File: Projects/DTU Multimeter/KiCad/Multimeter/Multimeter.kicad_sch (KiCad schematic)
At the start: 10 parts, among them U1 MCP3208-CI_P, U2 CD74HC4067E, U3 CD4053BE, U4 LM358P, U5 LM311N, U6 NE555P, U7 LM35DZ, U8 DS1307+

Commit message: Add schematic generator and update measured resistor values
Add generate_schematic.py using kicad-skip + sexpdata to programmatically
inject all passive components, net labels, power symbols, and group
annotations into the KiCad schematic. Moves existing ICs to a spread-out
layout via raw S-expression tree manipulation. Update config.h and build
guide with actual measured resistor values.
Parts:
- added BT1: CR2032, Battery:BatteryHolder_Keystone_3034_1x20mm, symbol Device:Battery_Cell
- added BZ1: Piezo, Buzzer_Beeper:Buzzer_12x9.5RM7.6, symbol Device:Buzzer
- added C1, C2, C3, C7, C8: 100n, Capacitor_THT:C_Disc_D5.0mm_W2.5mm_P2.50mm, symbol Device:C
- added C4, C5, C6: 10u, Capacitor_THT:CP_Radial_D5.0mm_P2.50mm, symbol Device:C_Polarized
- added D1: Red, LED_THT:LED_D3.0mm, symbol Device:LED
- added D2: Green, LED_THT:LED_D3.0mm, symbol Device:LED
- added D3: Yellow, LED_THT:LED_D3.0mm, symbol Device:LED
- added F1: 10A, Fuse:Fuseholder_Clip-5x20mm_Keystone_3517_Inline_P23.11x6.76mm_D1.70mm_Horizontal, symbol Device:Fuse
- added F2: 500mA, Fuse:Fuseholder_Clip-5x20mm_Keystone_3517_Inline_P23.11x6.76mm_D1.70mm_Horizontal, symbol Device:Fuse
- added R1: 50.15, Resistor_THT:R_Axial_DIN0207_L6.3mm_D2.5mm_P10.16mm_Horizontal, symbol Device:R
- added R10: 998, Resistor_THT:R_Axial_DIN0207_L6.3mm_D2.5mm_P10.16mm_Horizontal, symbol Device:R
- added R11: 99.49, Resistor_THT:R_Axial_DIN0207_L6.3mm_D2.5mm_P10.16mm_Horizontal, symbol Device:R
- added R12: 10.04, Resistor_THT:R_Axial_DIN0207_L6.3mm_D2.5mm_P10.16mm_Horizontal, symbol Device:R
- added R13: 1.05, Resistor_THT:R_Axial_DIN0207_L6.3mm_D2.5mm_P10.16mm_Horizontal, symbol Device:R
- added R14: 0.145, Resistor_THT:R_Axial_DIN0207_L6.3mm_D2.5mm_P10.16mm_Horizontal, symbol Device:R
- added R15: 1.002M, Resistor_THT:R_Axial_DIN0207_L6.3mm_D2.5mm_P10.16mm_Horizontal, symbol Device:R
- added R16: 100k, Resistor_THT:R_Axial_DIN0207_L6.3mm_D2.5mm_P10.16mm_Horizontal, symbol Device:R
- added R17: 1.003M, Resistor_THT:R_Axial_DIN0207_L6.3mm_D2.5mm_P10.16mm_Horizontal, symbol Device:R
- added R18, R22, R23, R24, R28, R29, R9: 10k, Resistor_THT:R_Axial_DIN0207_L6.3mm_D2.5mm_P10.16mm_Horizontal, symbol Device:R
- added R19: 99.48, Resistor_THT:R_Axial_DIN0207_L6.3mm_D2.5mm_P10.16mm_Horizontal, symbol Device:R
- added R2: 497, Resistor_THT:R_Axial_DIN0207_L6.3mm_D2.5mm_P10.16mm_Horizontal, symbol Device:R
- added R20: 9.09k, Resistor_THT:R_Axial_DIN0207_L6.3mm_D2.5mm_P10.16mm_Horizontal, symbol Device:R
- added R21: 1k, Resistor_THT:R_Axial_DIN0207_L6.3mm_D2.5mm_P10.16mm_Horizontal, symbol Device:R
- added R25, R26, R27: 330, Resistor_THT:R_Axial_DIN0207_L6.3mm_D2.5mm_P10.16mm_Horizontal, symbol Device:R
- added R3: 4990, Resistor_THT:R_Axial_DIN0207_L6.3mm_D2.5mm_P10.16mm_Horizontal, symbol Device:R
- added R4: 48.536k, Resistor_THT:R_Axial_DIN0207_L6.3mm_D2.5mm_P10.16mm_Horizontal, symbol Device:R
- added R5: 498k, Resistor_THT:R_Axial_DIN0207_L6.3mm_D2.5mm_P10.16mm_Horizontal, symbol Device:R
- added R6: 4.755M, Resistor_THT:R_Axial_DIN0207_L6.3mm_D2.5mm_P10.16mm_Horizontal, symbol Device:R
- added R7: 10.06M, Resistor_THT:R_Axial_DIN0207_L6.3mm_D2.5mm_P10.16mm_Horizontal, symbol Device:R
- added R8: 10.03M, Resistor_THT:R_Axial_DIN0207_L6.3mm_D2.5mm_P10.16mm_Horizontal, symbol Device:R
- added SW1: MODE, Button_Switch_THT:SW_PUSH_6mm, symbol Switch:SW_Push
- added SW2: FUNC, Button_Switch_THT:SW_PUSH_6mm, symbol Switch:SW_Push
- added SW3: RANGE, Button_Switch_THT:SW_PUSH_6mm, symbol Switch:SW_Push
- added SW4: SELECT, Button_Switch_THT:SW_PUSH_6mm, symbol Switch:SW_Push
- added Y1: 32.768kHz, Crystal:Crystal_C38-LF_D3.0mm_L8.0mm_Horizontal, symbol Device:Crystal
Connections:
- net GND: now reaches U6.1 (GND)
- net GND: now also U7.3 (GND)
- net VCC: now reaches U6.8 (VCC)
- net VCC: now also U7.1 (+VS)
- net ADC_CH5: now reaches U7.2 (VOUT)
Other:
- note added: "ADC (U1 MCP3208)"
- note added: "ANALOG MUX (U2 74HC4067 + Ref R1-R8)"
- note added: "CURRENT MUX (U3 CD4053 + Shunts R9-R14)"
- note added: "CURRENT SOURCE (U6 NE555 + C8, R17-R19)"
- note added: "DECOUPLING (C1-C6 near each IC)"
- note added: "DISPLAY (OLED 128x64, DS)"
- note added: "FREQUENCY COUNTER (U5 LM311 + R22-R24, C7)"
- note added: "I2C BUS (Pull-ups R28-R29)"
- note added: "INPUT PROTECTION (Fuses F1-F2 + Voltage Divider R15-R16)"
- note added: "RTC (U8 DS1307 + Crystal Y1 + Battery BT1)"
- note added: "SIGNAL CONDITIONING (U4 LM358 + R20-R21)"
- note added: "TEMPERATURE (U7 LM35)"
- note added: "USER INTERFACE (Buttons SW1-SW4, LEDs D1-D3, Buzzer BZ1)"
- moved on the sheet: A1, DS1, U1, U2, U3, U4A, U4B, U4C, U5, U6, U7, U8

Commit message: Wire R1-R8, R9-R14 and fix ERC errors
- Wire R1-R8 probe-input side to ADC_CH2 net (bus wire + junctions)
- Wire R9-R14 fuse-terminal side with FUSE_mA/FUSE_10A labels
- Fix ERC: relocate TERM labels, remove orphaned #PWR026,
  add 57 no-connect flags on unused A1 pins, add PWR_FLAG
  symbols on VCC/GND/VBAT nets
- Add schematic wiring guide
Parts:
- added D4: 1N4148, Diode_THT:D_DO-35_SOD27_P7.62mm_Horizontal, symbol Device:D
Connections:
- net ADC_CH1: now also R15.2, R16.1, U1.2 (CH1)
- net ADC_CH2: now also R1.1, R15.1, R2.1, R3.1, R4.1, R5.1, R6.1, R7.1, R8.1, U1.3 (CH2)
- net ADC_CH3: now also R20.2, U1.4 (CH3), U4.1
- net ADC_CH4: now also U1.5 (CH4), U4.7, D4.1 (K)
- net ADC_CH5: now also U1.6 (CH5)
- net BTN_FUNC: now also A1.AD4, SW2.1
- net BTN_MODE: now also A1.AD3, SW1.1
- net BTN_RANGE: now also A1.AD5, SW3.1
- net BTN_SEL: now also A1.AD6, SW4.1
- net BUZZER: now also A1.AD7, BZ1.1 (+)
- net CAP_CHG: now also A1.31, U6.3 (OUT)
- net CAP_DIS: now also A1.32
- net CUR_A: now also A1.27, U3.11 (A)
- net CUR_B: now also A1.28, U3.10 (B)
- net CUR_C: now also A1.29, U3.9 (C)
- net CUR_INH: now also A1.30, U3.6 (INH)
- net FREQ_IN: now also A1.AD2, R24.2, U5.7 (OUT)
- net GND: now also A1.GND2, BT1.2 (-), BZ1.2 (-), C1.2, C2.2, C3.2, C4.2, C5.2, C6.2, C8.2, D1.1 (K), D2.1 (K), D3.1 (K), DS1.2 (GND), R16.2, R21.2, R23.2, SW1.2, SW2.2, SW3.2, SW4.2, U1.14 (AGND), U1.9 (DGND), U2.12 (GND), U3.7 (VEE), U3.8 (VSS), U4.4 (GND), U5.1 (GND), U5.4 (VCC-), U8.4 (GND)
- net I2C_SCL: now also A1.SCL, DS1.3 (SCK), R29.2, U8.6 (SCL)
- net I2C_SDA: now also A1.SDA, DS1.4 (SDA), R28.2, U8.5 (SDA)
- net ISRC_EN: now also A1.33, U6.4 (RESET)
- net LED_GRN: now also A1.AD9, R26.1
- net LED_RED: now also A1.AD8, R25.1
- net LED_YEL: now also A1.AD10, R27.1
- net MUX_COM: now also U1.1 (CH0), U2.1 (COM)
- net MUX_EN: now also A1.26, U2.15 (~{E})
- net MUX_S0: now also A1.22, U2.10 (S0)
- net MUX_S1: now also A1.23, U2.11 (S1)
- net MUX_S2: now also A1.24, U2.14 (S2)
- net MUX_S3: now also A1.25, U2.13 (S3)
- net SPI_CS: now also A1.53, U1.10 (~CS/SHDN)
- net SPI_MISO: now also A1.50, U1.12 (DOUT)
- net SPI_MOSI: now also A1.51, U1.11 (DIN)
- net SPI_SCK: now also A1.52, U1.13 (CLK)
- net VCC: now also A1.5V_1 (+5V_1), C1.1, C2.1, C3.1, C4.1, C5.1, C6.1, DS1.1 (VDD), R22.1, R24.1, R28.1, R29.1, U1.15 (VREF), U1.16 (VDD), U2.24 (VCC), U3.16 (VDD), U4.8 (VCC), U5.8 (VCC+), U8.8 (VCC)
- net at R1.2: now also U2.9 (I0)
- net at D3.2 (A): now also R27.2
- net at C7.1: now also U5.2 (POS)
- net at U2.2 (I7): now also R8.2
- net at U2.3 (I6): now also R7.2
- net at U2.4 (I5): now also R6.2
- net at U2.5 (I4): now also R5.2
- net at U2.6 (I3): now also R4.2
- net at U2.7 (I2): now also R3.2
- net at U2.8 (I1): now also R2.2
- net FUSE_mA: now reaches R9.1
- net FUSE_mA: now also F2.2, R10.1, R11.2, R12.1, R13.1
- net at R9.2: now also U3.12 (AX_IN/OUT)
- net at D1.2 (A): now also R25.2
- net at R12.2: now also U3.3 (IN/OUT_CY)
- net at C8.1: now also U6.5 (CONT)
- net TMR_CAP: now reaches R18.2
- net TMR_CAP: now also R17.2, R19.2, U6.2 (TRIG), U6.6 (THRES)
- net at R17.1: now also R19.1, U6.7 (DISCH)
- net at D2.2 (A): now also R26.2
- net TERM_10A: now reaches F1.1
- net FUSE_10A: now reaches F1.2
- net FUSE_10A: now also R14.1
- net at R10.2: now also U3.13 (AY_IN/OUT)
- net at R20.1: now also R21.1, U4.2
- net at U4.6: now also D4.2 (A)
- net at R14.2: now also U3.1 (IN/OUT_BY)
- net at R23.1: now also R22.2, U5.3 (NEG)
- net at Y1.1: now also U8.2 (X2)
- net at Y1.2: now also U8.1 (X1)
- net SHUNT_NODE: now reaches U3.14 (OUT/IN_AX_OR_AY)
- net SHUNT_NODE: now also U3.15 (OUT/IN_BX_OR_BY), U3.4 (OUT/IN_CX_OR_CY), U4.3
- net at U3.2 (IN/OUT_BX): now also R13.2
- net at U3.5 (IN/OUT_CX): now also R11.1
- net at U8.3 (VBAT): now also BT1.1 (+)
- net TERM_mA: now reaches F2.1
- no-connect marks 0 -> 70
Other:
- moved on the sheet: BZ1, C2, C3, C4, C5, C6, C8, D1, D2, D3, F1, F2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

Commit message: Update DTU Multimeter PCB layout, schematic, and build guide
Add KiCad schematic fix scripts, ERC report, design plans,
and PlatformIO project configuration.
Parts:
- added J1, J2: Conn_01x01_Pin, Connector:Banana_Jack_1Pin, symbol Connector:Conn_01x01_Pin
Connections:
- net TMR_CAP is gone; now on net CAP_DIS: R17.2, R18.2, R19.2, U6.2 (TRIG), U6.6 (THRES)
- net ADC_CH2: now also C7.2, U4.5
- net ADC_CH4: now also D4.2 (A), U4.6
- net TERM_10A: now also J1.1 (Pin_1)
- net TERM_mA: now also J2.1 (Pin_1)
- net at R18.1: now also R17.1, R19.1, U6.7 (DISCH)
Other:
- moved on the sheet: A1, BT1, BZ1, C1, C2, C3, C4, C5, C6, C7, C8, D1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

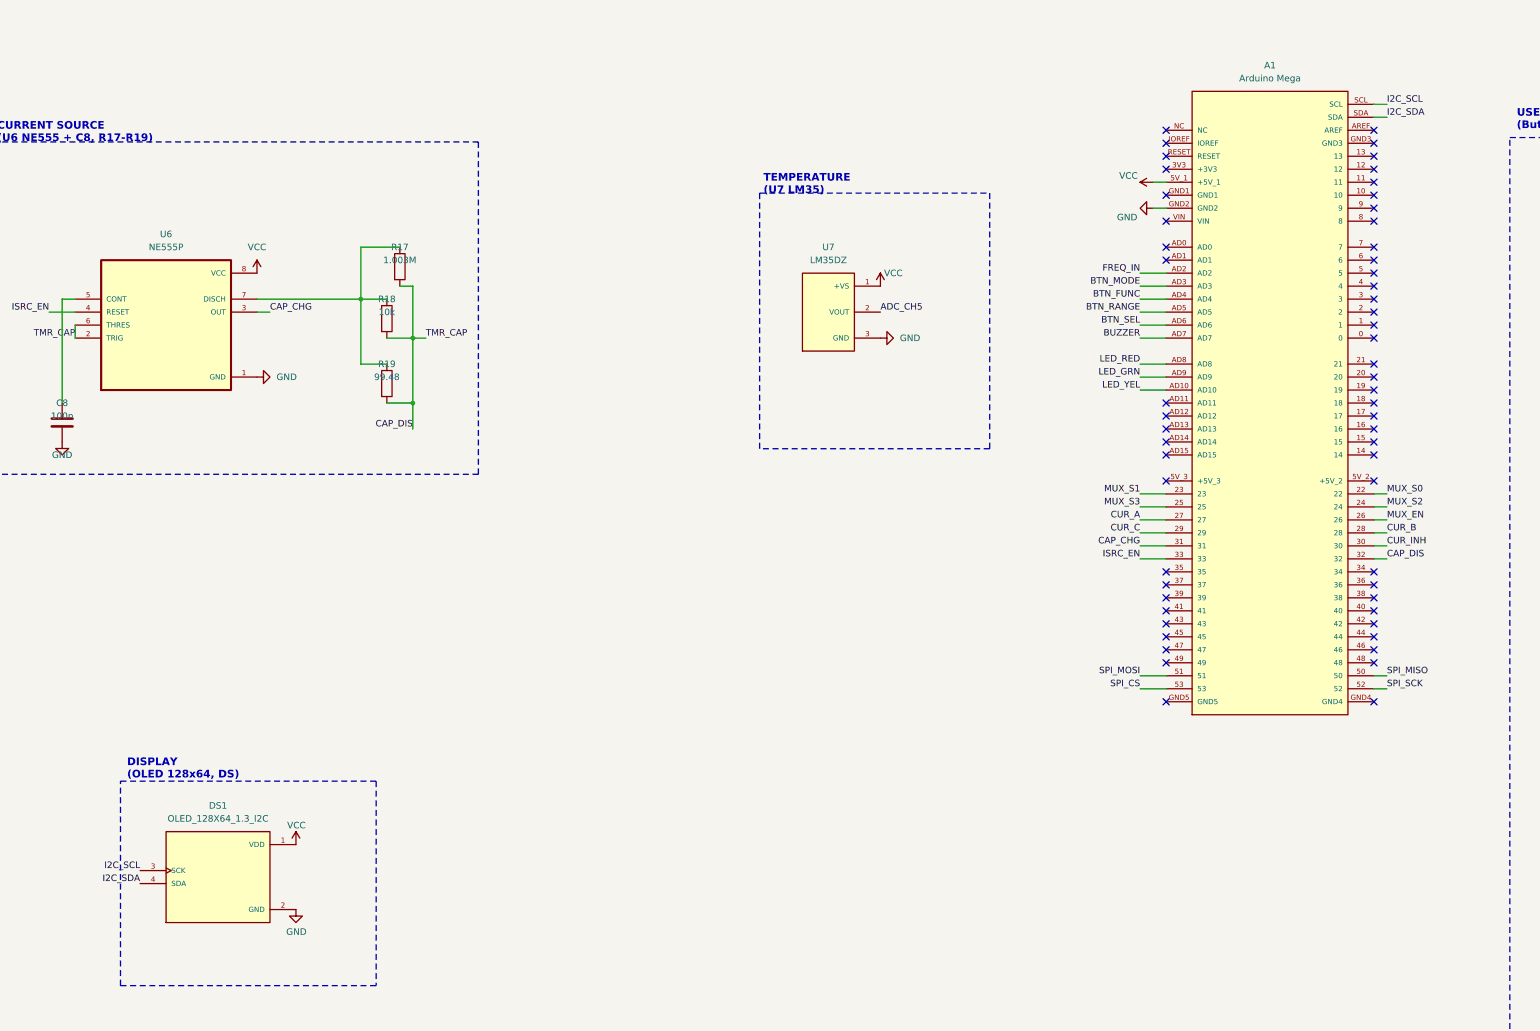
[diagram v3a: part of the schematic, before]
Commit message: multimeter: snapshot full design before v1 simplification
Captures the current full-featured multimeter state:
- Complete schematic with all 22 measurement modes
- PCB placement with all ICs and passives
- Breadboard test firmware (voltage/resistance)
- Updated Mega footprint (proper headers + Z offset)
- New OLED footprint/symbol/3D model
- DTU single-sided PCB rules applied

This commit is the base for the full-version-multimeter branch.
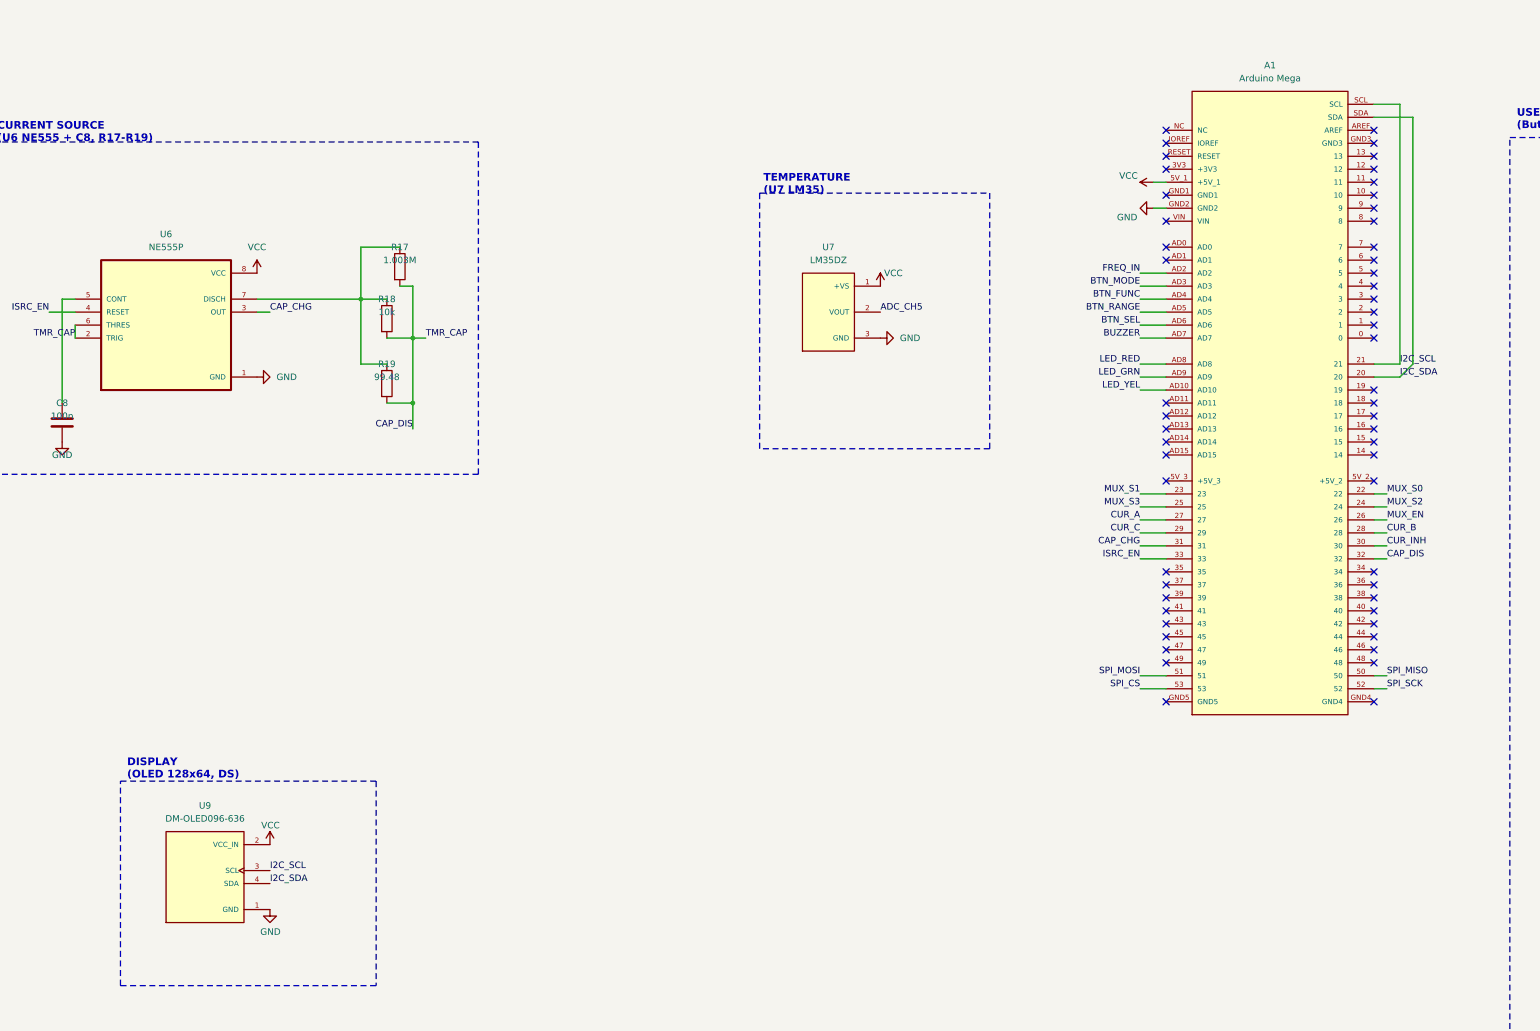
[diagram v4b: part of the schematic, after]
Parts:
- removed DS1: OLED_128X64_1.3_I2C, OLED_128X64_1.3_I2C:LCD_OLED_128X64_1.3_I2C, symbol OLED_128X64_1.3_I2C:OLED_128X64_1.3_I2C
- added U9: DM-OLED096-636, DM-OLED096-636:MODULE_DM-OLED096-636, symbol DM-OLED096-636:DM-OLED096-636
- F1, F2: footprint Fuse:Fuseholder_Clip-5x20mm_Keystone_3517_Inline_P23.11x6.76mm_D1.70mm_Horizontal -> Fuse:Fuseholder_Cylinder-5x20mm_Schurter_0031_8201_Horizontal_Open
- U2: footprint CD74HC4067E:DIP254P762X508-24 -> Package_DIP:DIP-24_18.0mmx34.29mm_W15.24mm
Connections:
- net GND: now also U9.1 (GND)
- net I2C_SCL: now also A1.21, U9.3 (SCL)
- net I2C_SDA: now also A1.20, U9.4 (SDA)
- net VCC: now also U9.2 (VCC_IN)
- no-connect marks 70 -> 68
